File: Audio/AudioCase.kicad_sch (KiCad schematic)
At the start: 6 parts, among them J1 PD給電, J2 入力ジャック, J3 出力ジャック, SW1 SW_Rotary_4x3

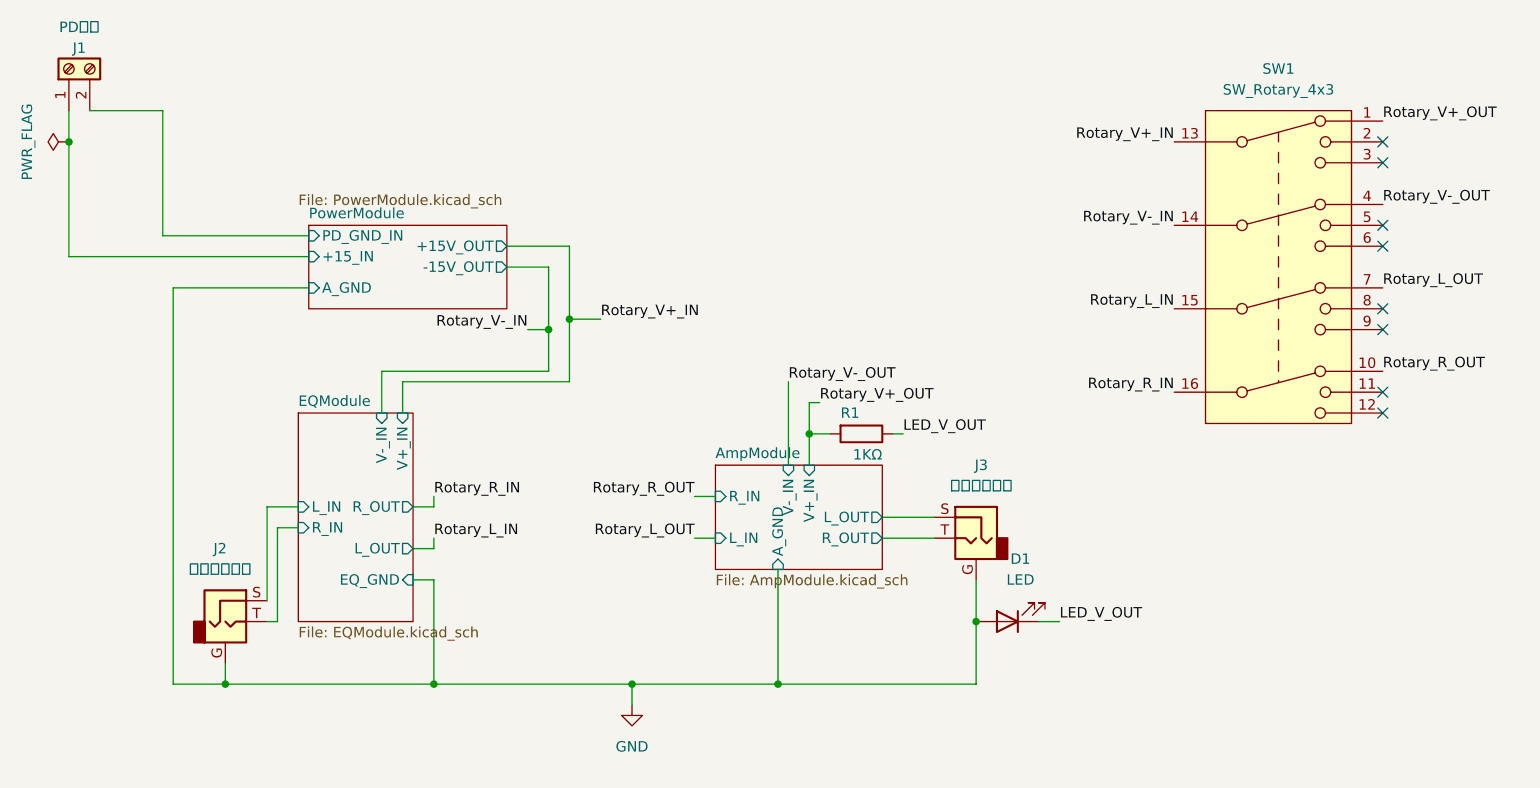
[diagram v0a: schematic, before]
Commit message: add controll module image
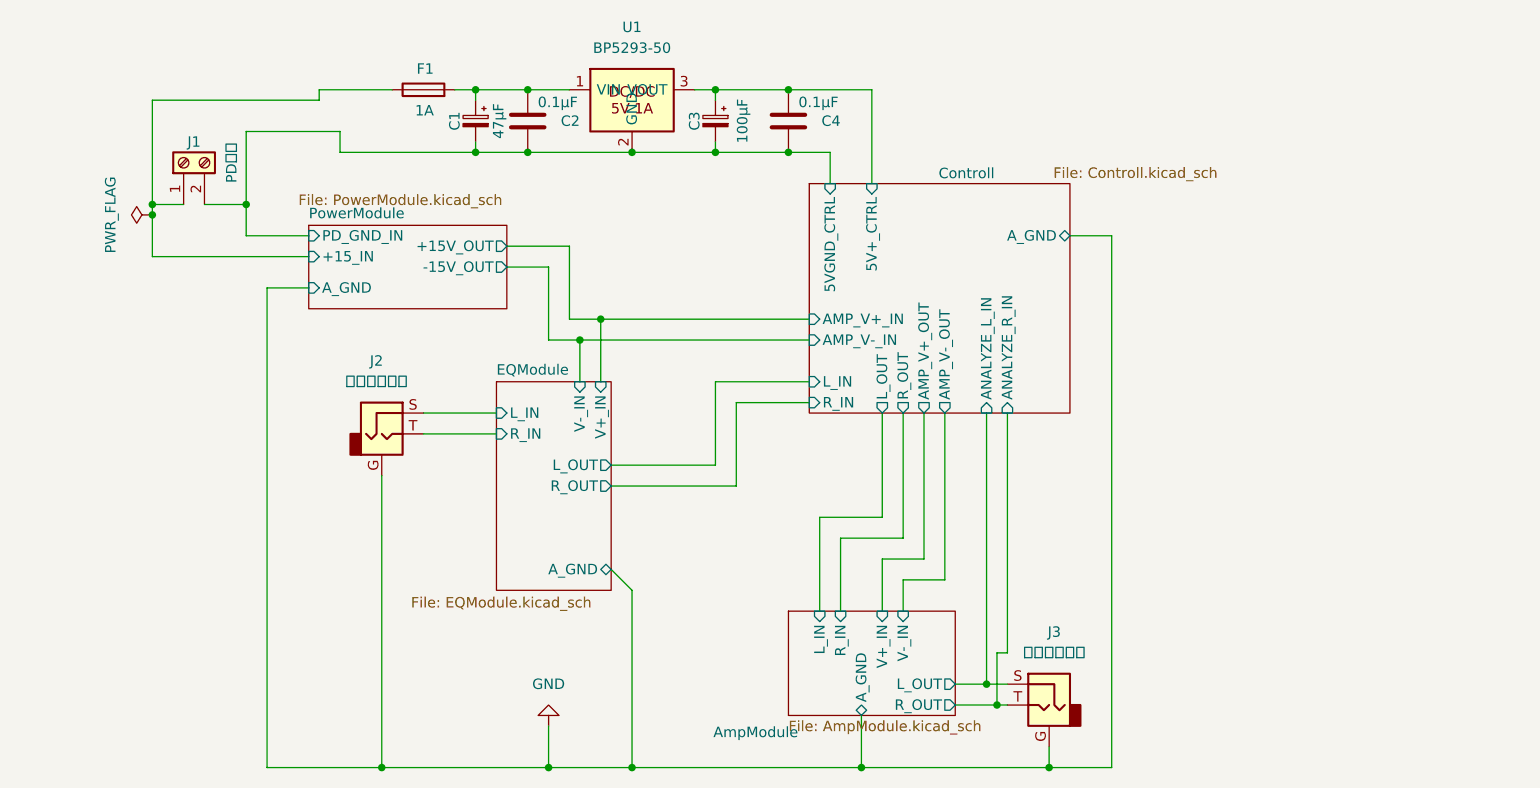
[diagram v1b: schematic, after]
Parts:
- removed D1: LED, TerminalBlock_Phoenix:TerminalBlock_Phoenix_MKDS-1,5-2-5.08_1x02_P5.08mm_Horizontal, symbol Device:LED
- removed R1: 1KΩ, Resistor_SMD:R_0603_1608Metric_Pad0.98x0.95mm_HandSolder, symbol Device:R
- removed SW1: SW_Rotary_4x3, symbol Switch:SW_Rotary_4x3
- added C1: 47μF, Capacitor_THT:CP_Radial_D8.0mm_P3.50mm, symbol Device:C_Polarized_Small
- added C2, C4: 0.1μF, Capacitor_THT:C_Disc_D5.0mm_W2.5mm_P2.50mm, symbol Device:C
- added C3: 100μF, Capacitor_THT:CP_Radial_D6.3mm_P2.50mm, symbol Device:C_Polarized_Small
- added F1: 1A, Resistor_THT:R_Axial_DIN0411_L9.9mm_D3.6mm_P12.70mm_Horizontal, symbol Device:Fuse
- added U1: BP5293-50, BP5293_ROHM:BP5293-50_ROHM_SIP-3, symbol BP5293-50:BP5293-50
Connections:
- net PowerModule/+15_IN: now also F1.1
- net PowerModule/PD_GND_IN renamed Controll/5VGND_CTRL
- net Controll/5VGND_CTRL: now also C1.2, C2.2, C3.2, C4.2, U1.2 (GND)
- new net: C1.1, C2.1, F1.2, U1.1 (VIN)
- new net Controll/5V+_CTRL: C3.1, C4.1, U1.3 (VOUT)
- no-connect marks 8 -> 0
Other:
- added sheet Controll (Controll.kicad_sch)
- sheet EQModule ports: added A_GND; removed EQ_GND
- moved on the sheet: J1, J2, J3

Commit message: rework pcb
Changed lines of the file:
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@@
+	)
+	(junction
+		(at 71.12 21.59)
+		(diameter 0)
+		(color 0 0 0 0)
 	)
 	(junction
@@
 	)
 	(junction
+		(at 34.29 35.56)
+		(diameter 0)
+		(color 0 0 0 0)
+	)
+	(junction
 		(at 71.12 29.21)
 		(diameter 0)
@@
 	)
 	(junction
-		(at 31.75 35.56)
-		(diameter 0)
-		(color 0 0 0 0)
-	)
-	(junction
 		(at 140.97 104.14)
 		(diameter 0)
@@
 	)
 	(junction
+		(at 68.58 21.59)
+		(diameter 0)
+		(color 0 0 0 0)
+	)
+	(junction
 		(at 80.01 104.14)
 		(diameter 0)
@@
 	)
 	(junction
-		(at 71.12 21.59)
+		(at 31.75 35.56)
 		(diameter 0)
 		(color 0 0 0 0)
 	)
-	(junction
-		(at 31.75 36.83)
-		(diameter 0)
-		(color 0 0 0 0)
-	)
 	(wire
 		(pts
@@
 	(wire
 		(pts
-			(xy 31.75 35.56) (xy 35.56 35.56)
+			(xy 31.75 35.56) (xy 34.29 35.56)
 		)
 		(stroke
@@
 	(wire
 		(pts
-			(xy 31.75 35.56) (xy 31.75 36.83)
+			(xy 31.75 35.56) (xy 31.75 41.91)
 		)
 		(stroke
@@
 	(wire
 		(pts
+			(xy 34.29 35.56) (xy 35.56 35.56)
+		)
+		(stroke
+			(width 0)
+			(type default)
+		)
+	)
+	(wire
+		(pts
 			(xy 115.57 76.2) (xy 115.57 85.09)
 		)
@@
 		(pts
 			(xy 71.12 29.21) (xy 54.61 29.21)
-		)
-		(stroke
-			(width 0)
-			(type default)
-		)
-	)
-	(wire
-		(pts
-			(xy 31.75 36.83) (xy 31.75 41.91)
 		)
 		(stroke
@@
 		(exclude_from_sim no)
 		(in_bom yes)
-		(on_board yes)
+		(on_board no)
 		(in_pos_files yes)
 		(dnp no)
@@
 		(exclude_from_sim no)
 		(in_bom yes)
-		(on_board yes)
+		(on_board no)
 		(in_pos_files yes)
 		(dnp no)
@@
 	(symbol
 		(lib_id "power:PWR_FLAG")
-		(at 31.75 36.83 90)
+		(at 34.29 35.56 180)
 		(unit 1)
 		(body_style 1)
@@
 		(dnp no)
 		(property "Reference" "#FLG01"
-			(at 29.845 36.83 0)
+			(at 34.29 37.465 0)
 			(hide yes)
 			(show_name no)
@@
 		)
 		(property "Value" "PWR_FLAG"
-			(at 26.67 36.83 0)
+			(at 24.892 38.608 0)
 			(show_name no)
 			(do_not_autoplace no)
@@
 		)
 		(property "Footprint" ""
-			(at 31.75 36.83 0)
+			(at 34.29 35.56 0)
 			(hide yes)
 			(show_name no)
@@
 		)
 		(property "Datasheet" ""
-			(at 31.75 36.83 0)
+			(at 34.29 35.56 0)
 			(hide yes)
 			(show_name no)
@@
 		)
 		(property "Description" "Special symbol for telling ERC where power comes from"
-			(at 31.75 36.83 0)
+			(at 34.29 35.56 0)
 			(hide yes)
 			(show_name no)
@@
 		(exclude_from_sim no)
 		(in_bom yes)
-		(on_board yes)
+		(on_board no)
 		(in_pos_files yes)
 		(dnp no)
@@
 		(exclude_from_sim no)
 		(in_bom yes)
-		(on_board yes)
+		(on_board no)
 		(in_pos_files yes)
 		(dnp no)
@@
 		(exclude_from_sim no)
 		(in_bom yes)
-		(on_board yes)
+		(on_board no)
 		(in_pos_files yes)
 		(dnp no)
@@
 		(exclude_from_sim no)
 		(in_bom yes)
-		(on_board yes)
+		(on_board no)
 		(in_pos_files yes)
 		(dnp no)
@@
 		(exclude_from_sim no)
 		(in_bom yes)
-		(on_board yes)
+		(on_board no)
 		(in_pos_files yes)
 		(dnp no)
@@
 				(path "/760b9589-09e7-434e-9ca2-6e4136e3b7a2"
 					(reference "C2")
+					(unit 1)
+				)
+			)
+		)
+	)
+	(symbol
+		(lib_id "power:PWR_FLAG")
+		(at 68.58 21.59 0)
+		(unit 1)
+		(body_style 1)
+		(exclude_from_sim no)
+		(in_bom yes)
+		(on_board yes)
+		(in_pos_files yes)
+		(dnp no)
+		(property "Reference" "#FLG08"
+			(at 68.58 19.685 0)
+			(hide yes)
+			(show_name no)
+			(do_not_autoplace no)
+			(effects
+				(font
+					(size 1.27 1.27)
+				)
+			)
+		)
+		(property "Value" "PWR_FLAG"
+			(at 77.978 18.542 0)
+			(show_name no)
+			(do_not_autoplace no)
+			(effects
+				(font
+					(size 1.27 1.27)
+				)
+			)
+		)
+		(property "Footprint" ""
+			(at 68.58 21.59 0)
+			(hide yes)
+			(show_name no)
+			(do_not_autoplace no)
+			(effects
+				(font
+					(size 1.27 1.27)
+				)
+			)
+		)
+		(property "Datasheet" ""
+			(at 68.58 21.59 0)
+			(hide yes)
+			(show_name no)
+			(do_not_autoplace no)
+			(effects
+				(font
+					(size 1.27 1.27)
+				)
+			)
+		)
+		(property "Description" "Special symbol for telling ERC where power comes from"
+			(at 68.58 21.59 0)
+			(hide yes)
+			(show_name no)
+			(do_not_autoplace no)
+			(effects
+				(font
+					(size 1.27 1.27)
+				)
+			)
+		)
+		(pin "1"
+		)
+		(instances
+			(project "AudioCase"
+				(path "/760b9589-09e7-434e-9ca2-6e4136e3b7a2"
+					(reference "#FLG08")
 					(unit 1)
 				)
@@
 		(exclude_from_sim no)
 		(in_bom yes)
-		(on_board yes)
+		(on_board no)
 		(in_pos_files yes)
 		(dnp no)
@@
 		(exclude_from_sim no)
 		(in_bom yes)
-		(on_board yes)
+		(on_board no)
 		(in_pos_files yes)
 		(dnp no)
@@
 		(exclude_from_sim no)
 		(in_bom yes)
-		(on_board yes)
+		(on_board no)
 		(dnp no)
 		(stroke

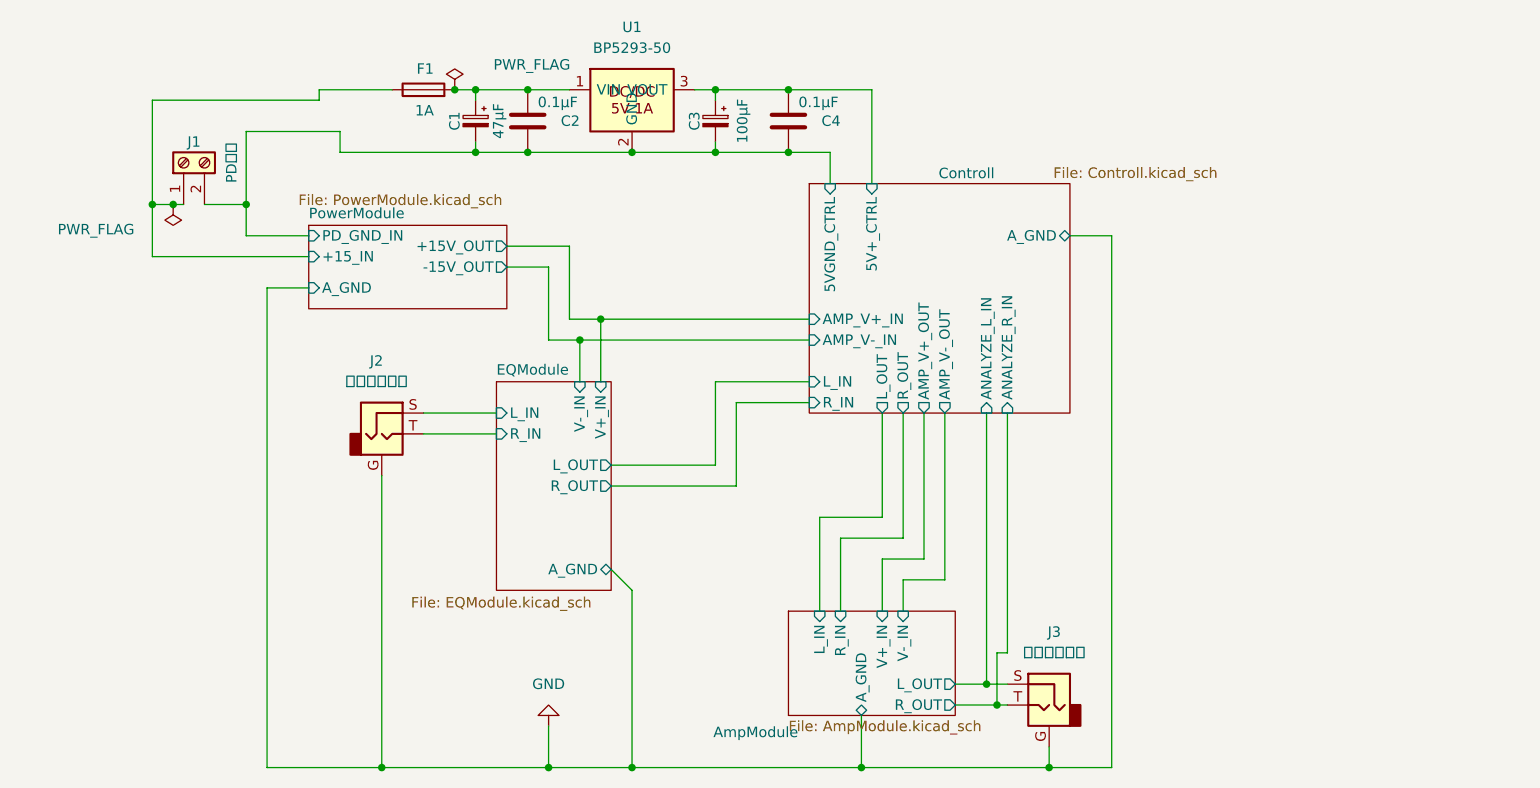
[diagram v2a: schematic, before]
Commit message: add relay
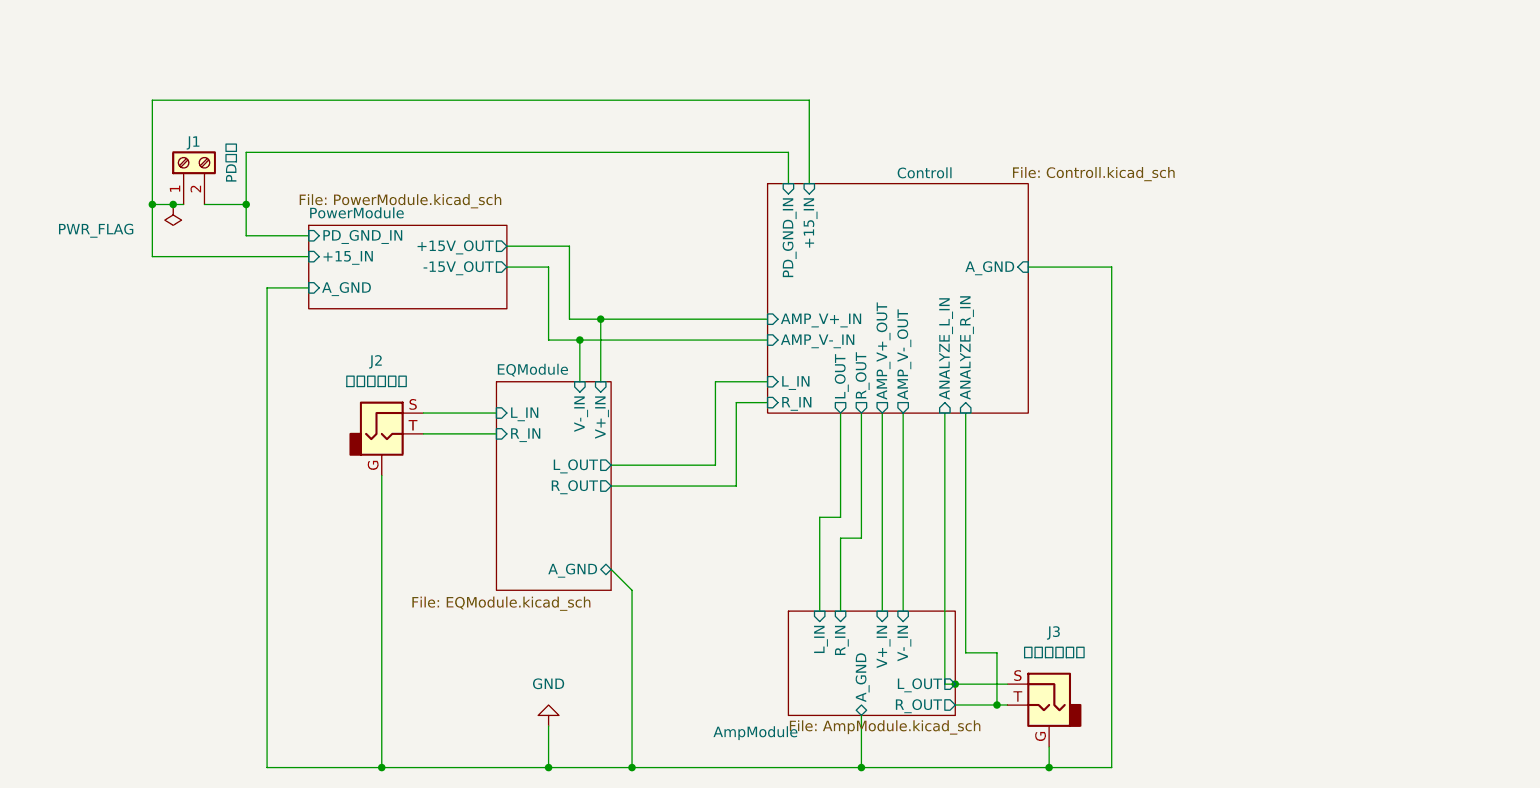
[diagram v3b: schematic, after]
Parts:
- removed C1: 47μF, Capacitor_THT:CP_Radial_D8.0mm_P3.50mm, symbol Device:C_Polarized_Small
- removed C2, C4: 0.1μF, Capacitor_THT:C_Disc_D5.0mm_W2.5mm_P2.50mm, symbol Device:C
- removed C3: 100μF, Capacitor_THT:CP_Radial_D6.3mm_P2.50mm, symbol Device:C_Polarized_Small
- removed F1: 1A, Resistor_THT:R_Axial_DIN0411_L9.9mm_D3.6mm_P12.70mm_Horizontal, symbol Device:Fuse
- removed U1: BP5293-50, BP5293_ROHM:BP5293-50_ROHM_SIP-3, symbol BP5293-50:BP5293-50
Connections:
- net Controll/5VGND_CTRL renamed Controll/PD_GND_IN
- net PowerModule/+15_IN renamed Controll/+15_IN
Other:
- sheet Controll ports: added +15_IN, PD_GND_IN; removed 5V+_CTRL, 5VGND_CTRL

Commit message: remove analyze
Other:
- sheet Controll ports: added none; removed ANALYZE_L_IN, ANALYZE_R_IN, A_GND
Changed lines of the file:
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@@
-	)
-	(junction
-		(at 140.97 104.14)
-		(diameter 0)
-		(color 0 0 0 0)
 	)
 	(junction
@@
 	)
 	(junction
-		(at 134.62 96.52)
-		(diameter 0)
-		(color 0 0 0 0)
-	)
-	(junction
 		(at 80.01 104.14)
 		(diameter 0)
@@
 		(color 0 0 0 0)
 	)
-	(junction
-		(at 129.54 93.98)
-		(diameter 0)
-		(color 0 0 0 0)
-	)
-	(wire
-		(pts
-			(xy 140.97 104.14) (xy 148.59 104.14)
-		)
-		(stroke
-			(width 0)
-			(type default)
-		)
-	)
 	(wire
 		(pts
@@
 	(wire
 		(pts
-			(xy 129.54 96.52) (xy 134.62 96.52)
-		)
-		(stroke
-			(width 0)
-			(type default)
-		)
-	)
-	(wire
-		(pts
 			(xy 87.63 80.01) (xy 90.17 82.55)
 		)
@@
 	(wire
 		(pts
-			(xy 134.62 96.52) (xy 135.89 96.52)
+			(xy 129.54 96.52) (xy 135.89 96.52)
 		)
 		(stroke
@@
 	(wire
 		(pts
-			(xy 128.27 93.98) (xy 129.54 93.98)
-		)
-		(stroke
-			(width 0)
-			(type default)
-		)
-	)
-	(wire
-		(pts
 			(xy 31.75 35.56) (xy 34.29 35.56)
 		)
@@
 	(wire
 		(pts
-			(xy 134.62 90.17) (xy 134.62 96.52)
-		)
-		(stroke
-			(width 0)
-			(type default)
-		)
-	)
-	(wire
-		(pts
 			(xy 31.75 35.56) (xy 31.75 41.91)
 		)
@@
 	(wire
 		(pts
-			(xy 130.81 90.17) (xy 134.62 90.17)
-		)
-		(stroke
-			(width 0)
-			(type default)
-		)
-	)
-	(wire
-		(pts
 			(xy 83.82 52.07) (xy 83.82 57.15)
 		)
@@
 	(wire
 		(pts
-			(xy 128.27 60.96) (xy 128.27 93.98)
-		)
-		(stroke
-			(width 0)
-			(type default)
-		)
-	)
-	(wire
-		(pts
 			(xy 120.65 60.96) (xy 120.65 85.09)
 		)
@@
 	(wire
 		(pts
-			(xy 130.81 60.96) (xy 130.81 90.17)
-		)
-		(stroke
-			(width 0)
-			(type default)
-		)
-	)
-	(wire
-		(pts
-			(xy 148.59 43.18) (xy 138.43 43.18)
-		)
-		(stroke
-			(width 0)
-			(type default)
-		)
-	)
-	(wire
-		(pts
 			(xy 86.36 49.53) (xy 106.68 49.53)
 		)
@@
 	(wire
 		(pts
+			(xy 129.54 93.98) (xy 135.89 93.98)
+		)
+		(stroke
+			(width 0)
+			(type default)
+		)
+	)
+	(wire
+		(pts
 			(xy 100.33 67.31) (xy 100.33 57.15)
 		)
@@
 	(wire
 		(pts
-			(xy 129.54 93.98) (xy 135.89 93.98)
-		)
-		(stroke
-			(width 0)
-			(type default)
-		)
-	)
-	(wire
-		(pts
 			(xy 100.33 57.15) (xy 106.68 57.15)
-		)
-		(stroke
-			(width 0)
-			(type default)
-		)
-	)
-	(wire
-		(pts
-			(xy 148.59 43.18) (xy 148.59 104.14)
 		)
 		(stroke
@@
 			(effects
 				(font
-					(size 1.27 1.27)
-				)
-				(justify left)
-			)
-		)
-		(pin "A_GND" input
-			(at 138.43 43.18 0)
-			(effects
-				(font
-					(size 1.27 1.27)
-				)
-				(justify right)
-			)
-		)
-		(pin "ANALYZE_L_IN" input
-			(at 128.27 60.96 270)
-			(effects
-				(font
-					(size 1.27 1.27)
-				)
-				(justify left)
-			)
-		)
-		(pin "ANALYZE_R_IN" input
-			(at 130.81 60.96 270)
-			(effects
-				(font
